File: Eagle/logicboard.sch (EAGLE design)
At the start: 28 parts, among them U2 ENC28J60-SO, U3 ATMEGA328P_PDIP, Y2 25MHz, Y3 16MHz

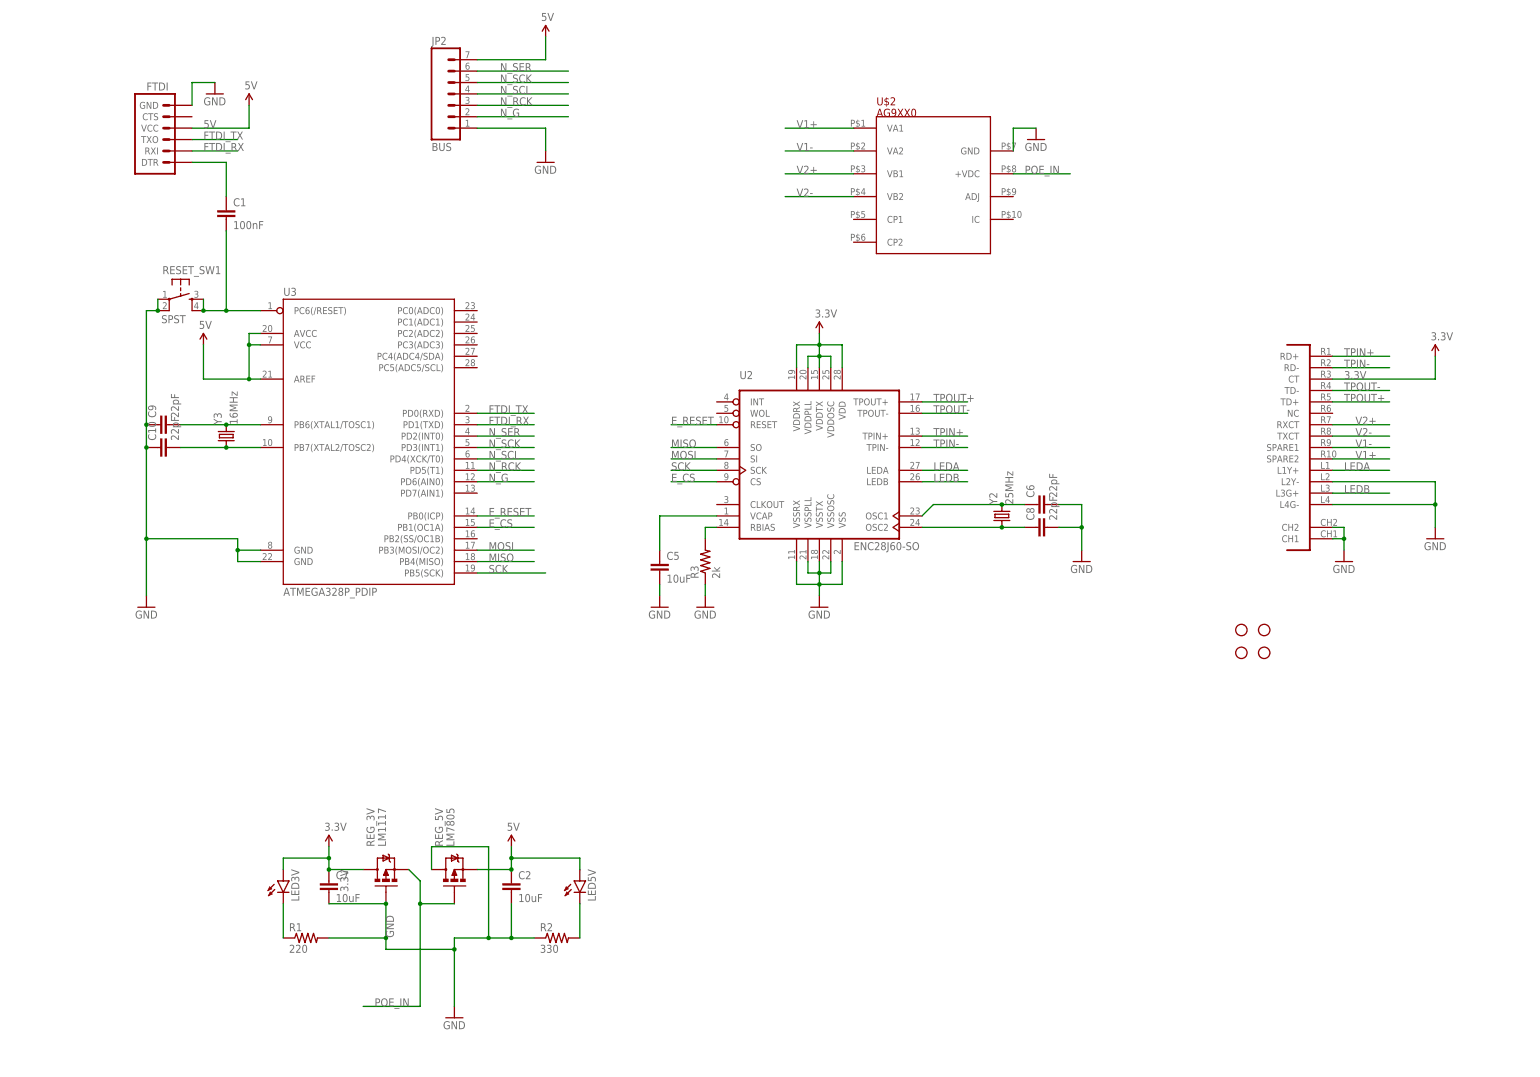
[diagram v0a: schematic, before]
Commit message: Update schematic to include on-board 200V psu
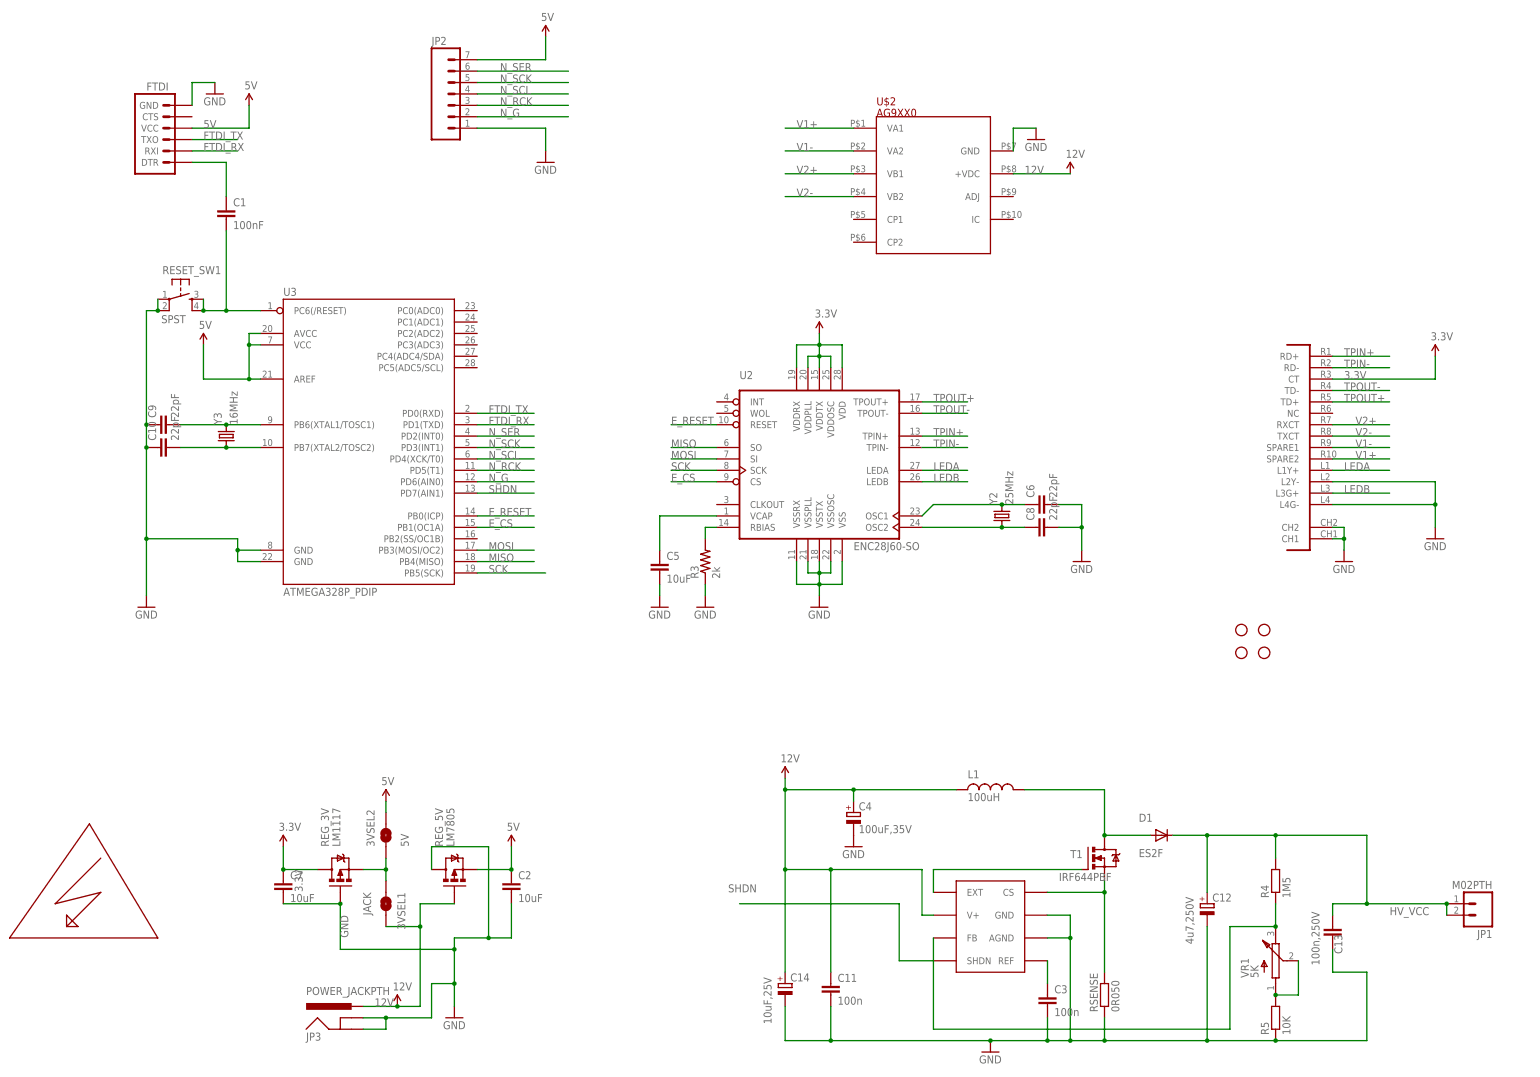
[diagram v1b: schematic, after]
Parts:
- removed LED3V, LED5V: (no value), SparkFun-LED:LED3MM
- removed R1: 220, SparkFun-Resistors:RESISTORPTH-1/4W-VERT
- removed R2: 330, SparkFun-Resistors:RESISTORPTH-1/4W-VERT
- added 3VSEL1: JACK, SparkFun-Passives:JUMPER-PAD-2-NOROUND
- added 3VSEL2: 5V, SparkFun-Passives:JUMPER-PAD-2-NOROUND
- added C11, C3: 100n, rcl:C-EUC0805
- added C12: 4u7,250V, nick:C-POL-EU-NICHICON-UJ-12
- added C13: 100n,250V, nick:C-EU-2420
- added C14: 10uF,25V, nick:C-POL-EU7343
- added C4: 100uF,35V, nick:C-POL-EU7343
- added D1: ES2F, diode:DIODE-SMC
- added JP1: M02PTH, SparkFun-Connectors:M02PTH
- added JP3: POWER_JACKPTH, SparkFun-Connectors:POWER_JACKPTH
- added L1: 100uH, nick:L-SMT-POWER-B82479
- added R4: 1M5, rcl:R-EU_R2512
- added R5: 10K, rcl:R-EU_R0805
- added RSENSE: 0R050, rcl:R-EU_R2010
- added T1: IRF644PBF, transistor-power:IRF740
- added U$1: MAX1771, max1771:MAX1771
- added U$4: HIGHVOLTAGE, highvoltage:HIGHVOLTAGE
- added VR1: 5K, nick:TRIMPOT-3214W
- JP2: value BUS -> (none)
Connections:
- removed net N$2: LED5V.C, R2.2
- removed net POE_IN: REG_3V.S, REG_5V.G, U$2.+VDC
- new net 12V: 3VSEL1.2, C11.1, C14.+, C4.+, JP3.PWR, L1.1, REG_5V.G, U$1.V+, U$2.+VDC
- new net EXT: T1.G, U$1.EXT
- new net HV_VCC: C12.+, C13.1, D1.C, JP1.1, JP1.2, R4.2
- new net N$10: C3.1, U$1.REF
- new net N$15: D1.A, L1.2, T1.D
- new net N$7: R5.2, VR1.A, VR1.W
- new net N$8: R4.1, U$1.FB, VR1.B
- new net N$9: RSENSE.2, T1.S, U$1.CS
- new net SHDN: U$1.SHDN, U3.PD7(AIN1)
- net 3.3V: no longer LED3V.A
- net 5V: now also 3VSEL2.2; no longer LED5V.A
- net GND: now also C11.2, C12.-, C13.2, C14.-, C3.2, C4.-, JP3.GND, JP3.GNDBREAK, R5.1, RSENSE.1, U$1.AGND, U$1.GND; no longer R1.2, R2.1
- net N$1: now also 3VSEL1.1, 3VSEL2.1, REG_3V.S; no longer LED3V.C, R1.1
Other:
- moved on the sheet: C7, REG_3V

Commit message: Ensure latest eagle
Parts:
- added G1: CR2032V, battery:CR2032V
- added Q1: (no value), crystal:CRYSTALTC26V
- added U$5: PT7C4302, Custom:PT7C4302
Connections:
- removed net N_G: JP2.2, U3.PD6(AIN0)
- removed net N_SCL: JP2.4, U3.PD4(XCK/T0)
- new net N$11: Q1.2, U$5.X1
- new net N$12: Q1.1, U$5.X2
- new net N$2: G1.+, U$5.VCC1
- new net RTC_CLK: U$5.SCLK, U3.PD4(XCK/T0)
- new net RTC_IO: U$5.IO, U3.PD6(AIN0)
- new net RTC_RST: U$5./RST, U3.PB2(SS/OC1B)
- net 5V: now also JP2.4, U$5.VCC2
- net GND: now also G1.-, JP2.2, U$5.GND
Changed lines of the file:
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@@
 <part name="3VSEL2" library="SparkFun-Passives" deviceset="JUMPER-PAD-2-NO" device="ROUND" value="5V"/>
 <part name="SUPPLY11" library="SparkFun-Aesthetics" deviceset="5V" device=""/>
+<part name="U$5" library="Custom" deviceset="PT7C4302" device=""/>
+<part name="Q1" library="crystal" deviceset="CRYSTAL" device="TC26V"/>
+<part name="GND11" library="SparkFun-Aesthetics" deviceset="GND" device=""/>
+<part name="SUPPLY12" library="SparkFun-Aesthetics" deviceset="5V" device=""/>
+<part name="SUPPLY13" library="SparkFun-Aesthetics" deviceset="5V" device=""/>
+<part name="G1" library="battery" deviceset="CR2032V" device=""/>
+<part name="GND15" library="SparkFun-Aesthetics" deviceset="GND" device=""/>
 </parts>
 <sheets>
@@
 <instance part="3VSEL2" gate="G$1" x="93.98" y="50.8" rot="R90"/>
 <instance part="SUPPLY11" gate="G$1" x="93.98" y="58.42"/>
+<instance part="U$5" gate="G$1" x="299.72" y="210.82"/>
+<instance part="Q1" gate="G$1" x="279.4" y="208.28" rot="R90"/>
+<instance part="GND11" gate="1" x="284.48" y="198.12"/>
+<instance part="SUPPLY12" gate="G$1" x="284.48" y="218.44"/>
+<instance part="SUPPLY13" gate="G$1" x="139.7" y="218.44"/>
+<instance part="G1" gate="1" x="335.28" y="213.36" rot="R180"/>
+<instance part="GND15" gate="1" x="345.44" y="205.74"/>
 </instances>
 <busses>
@@
 <segment>
 <pinref part="U3" gate="G$1" pin="PB5(SCK)"/>
-<wire x1="114.3" y1="109.22" x2="129.54" y2="109.22" width="0.1524" layer="91"/>
+<wire x1="114.3" y1="109.22" x2="127" y2="109.22" width="0.1524" layer="91"/>
 <label x="116.84" y="109.22" size="1.778" layer="95"/>
 </segment>
@@
 </segment>
 <segment>
-<wire x1="114.3" y1="208.28" x2="129.54" y2="208.28" width="0.1524" layer="91"/>
+<wire x1="114.3" y1="208.28" x2="119.38" y2="208.28" width="0.1524" layer="91"/>
+<wire x1="119.38" y1="208.28" x2="129.54" y2="208.28" width="0.1524" layer="91"/>
 <wire x1="129.54" y1="208.28" x2="129.54" y2="203.2" width="0.1524" layer="91"/>
 <pinref part="GND6" gate="1" pin="GND"/>
 <pinref part="JP2" gate="G$1" pin="1"/>
+<wire x1="114.3" y1="210.82" x2="119.38" y2="210.82" width="0.1524" layer="91"/>
+<pinref part="JP2" gate="G$1" pin="2"/>
+<wire x1="119.38" y1="210.82" x2="119.38" y2="208.28" width="0.1524" layer="91"/>
+<junction x="119.38" y="208.28"/>
 </segment>
 <segment>
@@
 <pinref part="GND7" gate="1" pin="GND"/>
 </segment>
+<segment>
+<pinref part="U$5" gate="G$1" pin="GND"/>
+<wire x1="287.02" y1="205.74" x2="284.48" y2="205.74" width="0.1524" layer="91"/>
+<wire x1="284.48" y1="205.74" x2="284.48" y2="200.66" width="0.1524" layer="91"/>
+<pinref part="GND11" gate="1" pin="GND"/>
+</segment>
+<segment>
+<pinref part="G1" gate="1" pin="-"/>
+<wire x1="340.36" y1="213.36" x2="345.44" y2="213.36" width="0.1524" layer="91"/>
+<wire x1="345.44" y1="213.36" x2="345.44" y2="208.28" width="0.1524" layer="91"/>
+<pinref part="GND15" gate="1" pin="GND"/>
+</segment>
 </net>
 <net name="E_CS" class="0">
@@
 <wire x1="93.98" y1="58.42" x2="93.98" y2="55.88" width="0.1524" layer="91"/>
 </segment>
+<segment>
+<pinref part="U$5" gate="G$1" pin="VCC2"/>
+<wire x1="287.02" y1="213.36" x2="284.48" y2="213.36" width="0.1524" layer="91"/>
+<wire x1="284.48" y1="213.36" x2="284.48" y2="218.44" width="0.1524" layer="91"/>
+<pinref part="SUPPLY12" gate="G$1" pin="5V"/>
+</segment>
+<segment>
+<wire x1="114.3" y1="215.9" x2="139.7" y2="215.9" width="0.1524" layer="91"/>
+<label x="119.38" y="215.9" size="1.778" layer="95"/>
+<pinref part="JP2" gate="G$1" pin="4"/>
+<pinref part="SUPPLY13" gate="G$1" pin="5V"/>
+<wire x1="139.7" y1="215.9" x2="139.7" y2="218.44" width="0.1524" layer="91"/>
+</segment>
 </net>
 <net name="N$37" class="0">
@@
 </segment>
 </net>
-<net name="N_SCL" class="0">
-<segment>
-<wire x1="114.3" y1="215.9" x2="134.62" y2="215.9" width="0.1524" layer="91"/>
-<label x="119.38" y="215.9" size="1.778" layer="95"/>
-<pinref part="JP2" gate="G$1" pin="4"/>
-</segment>
-<segment>
-<wire x1="127" y1="134.62" x2="114.3" y2="134.62" width="0.1524" layer="91"/>
-<label x="116.84" y="134.62" size="1.778" layer="95"/>
-<pinref part="U3" gate="G$1" pin="PD4(XCK/T0)"/>
-</segment>
-</net>
 <net name="N_RCK" class="0">
 <segment>
@@
 <label x="116.84" y="132.08" size="1.778" layer="95"/>
 <pinref part="U3" gate="G$1" pin="PD5(T1)"/>
-</segment>
-</net>
-<net name="N_G" class="0">
-<segment>
-<wire x1="114.3" y1="210.82" x2="134.62" y2="210.82" width="0.1524" layer="91"/>
-<label x="119.38" y="210.82" size="1.778" layer="95"/>
-<pinref part="JP2" gate="G$1" pin="2"/>
-</segment>
-<segment>
-<wire x1="127" y1="129.54" x2="114.3" y2="129.54" width="0.1524" layer="91"/>
-<label x="116.84" y="129.54" size="1.778" layer="95"/>
-<pinref part="U3" gate="G$1" pin="PD6(AIN0)"/>
 </segment>
 </net>
@@
 </segment>
 </net>
+<net name="N$11" class="0">
+<segment>
+<pinref part="U$5" gate="G$1" pin="X1"/>
+<pinref part="Q1" gate="G$1" pin="2"/>
+<wire x1="287.02" y1="210.82" x2="279.4" y2="210.82" width="0.1524" layer="91"/>
+</segment>
+</net>
+<net name="N$12" class="0">
+<segment>
+<pinref part="Q1" gate="G$1" pin="1"/>
+<wire x1="279.4" y1="205.74" x2="281.94" y2="205.74" width="0.1524" layer="91"/>
+<wire x1="281.94" y1="205.74" x2="281.94" y2="208.28" width="0.1524" layer="91"/>
+<pinref part="U$5" gate="G$1" pin="X2"/>
+<wire x1="281.94" y1="208.28" x2="287.02" y2="208.28" width="0.1524" layer="91"/>
+</segment>
+</net>
+<net name="N$2" class="0">
+<segment>
+<pinref part="U$5" gate="G$1" pin="VCC1"/>
+<wire x1="314.96" y1="213.36" x2="330.2" y2="213.36" width="0.1524" layer="91"/>
+<pinref part="G1" gate="1" pin="+"/>
+</segment>
+</net>
+<net name="RTC_CLK" class="0">
+<segment>
+<pinref part="U$5" gate="G$1" pin="SCLK"/>
+<wire x1="314.96" y1="210.82" x2="327.66" y2="210.82" width="0.1524" layer="91"/>
+<label x="317.5" y="210.82" size="1.778" layer="95"/>
+</segment>
+<segment>
+<wire x1="114.3" y1="134.62" x2="127" y2="134.62" width="0.1524" layer="91"/>
+<label x="116.84" y="134.62" size="1.778" layer="95"/>
+<pinref part="U3" gate="G$1" pin="PD4(XCK/T0)"/>
+</segment>
+</net>
+<net name="RTC_IO" class="0">
+<segment>
+<pinref part="U$5" gate="G$1" pin="IO"/>
+<wire x1="314.96" y1="208.28" x2="327.66" y2="208.28" width="0.1524" layer="91"/>
+<label x="317.5" y="208.28" size="1.778" layer="95"/>
+</segment>
+<segment>
+<wire x1="114.3" y1="129.54" x2="127" y2="129.54" width="0.1524" layer="91"/>
+<label x="116.84" y="129.54" size="1.778" layer="95"/>
+<pinref part="U3" gate="G$1" pin="PD6(AIN0)"/>
+</segment>
+</net>
+<net name="RTC_RST" class="0">
+<segment>
+<pinref part="U$5" gate="G$1" pin="/RST"/>
+<wire x1="314.96" y1="205.74" x2="327.66" y2="205.74" width="0.1524" layer="91"/>
+<label x="317.5" y="205.74" size="1.778" layer="95"/>
+</segment>
+<segment>
+<wire x1="114.3" y1="116.84" x2="127" y2="116.84" width="0.1524" layer="91"/>
+<label x="116.84" y="116.84" size="1.778" layer="95"/>
+<pinref part="U3" gate="G$1" pin="PB2(SS/OC1B)"/>
+</segment>
+</net>
